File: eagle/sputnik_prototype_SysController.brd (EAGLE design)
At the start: 99 x 100 mm, 73 parts, among them IC1 74HC4067, Q1 IRLML6344TRPBF, SW1 TPS25944LRVCRWQFN-20-3X4, U1 MEGA128-A, X1 CRYSTAL-ABRACON-ABM3-SMD

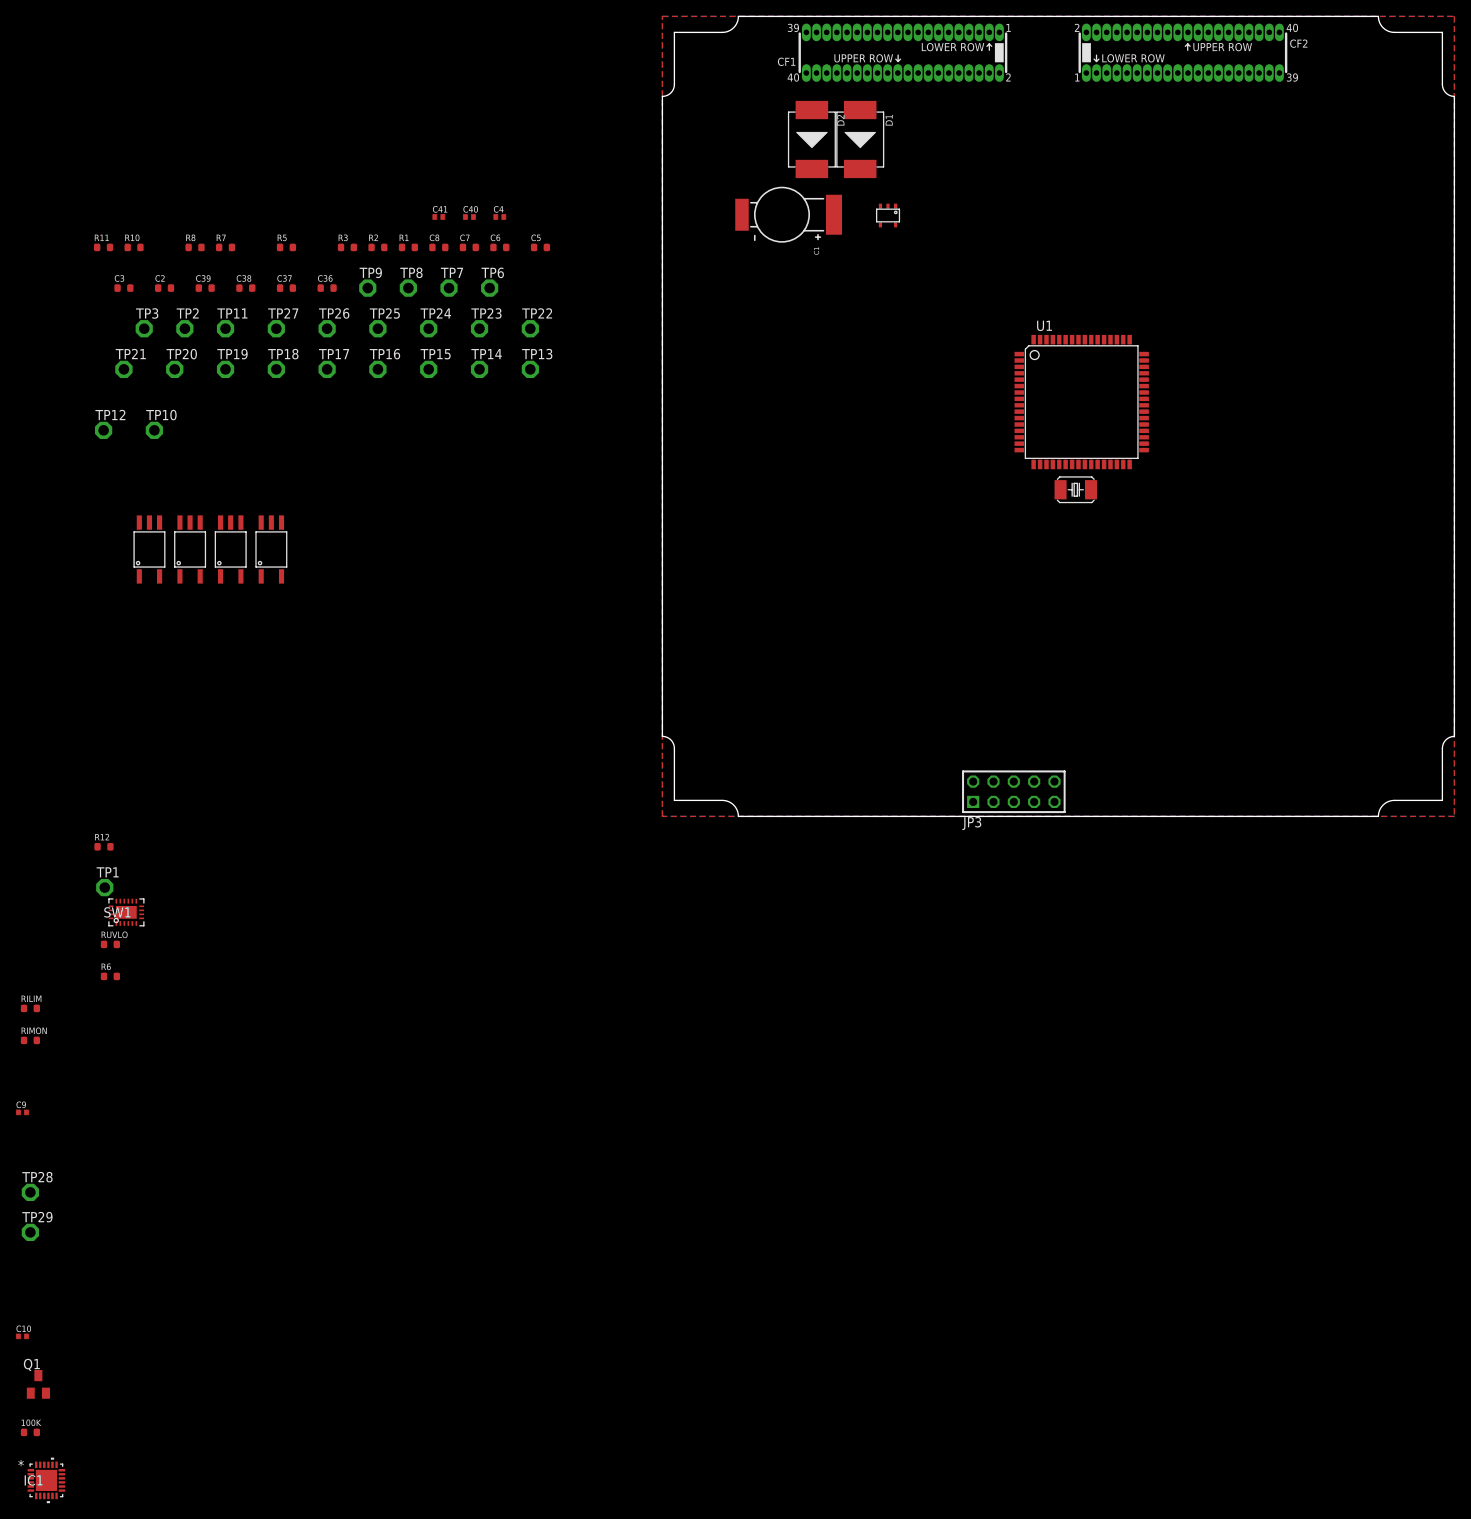
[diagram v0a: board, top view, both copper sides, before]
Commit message: Added DNP LEDs and MOSFET drives to UARTs. Fixed TPS circuits with SOT-32-6 N/P MOSFET pair, which worked out nicely. Added another TPS to flesh it out, make sure it wasn't totally stupid. Added more DN LEDs to the outputs.
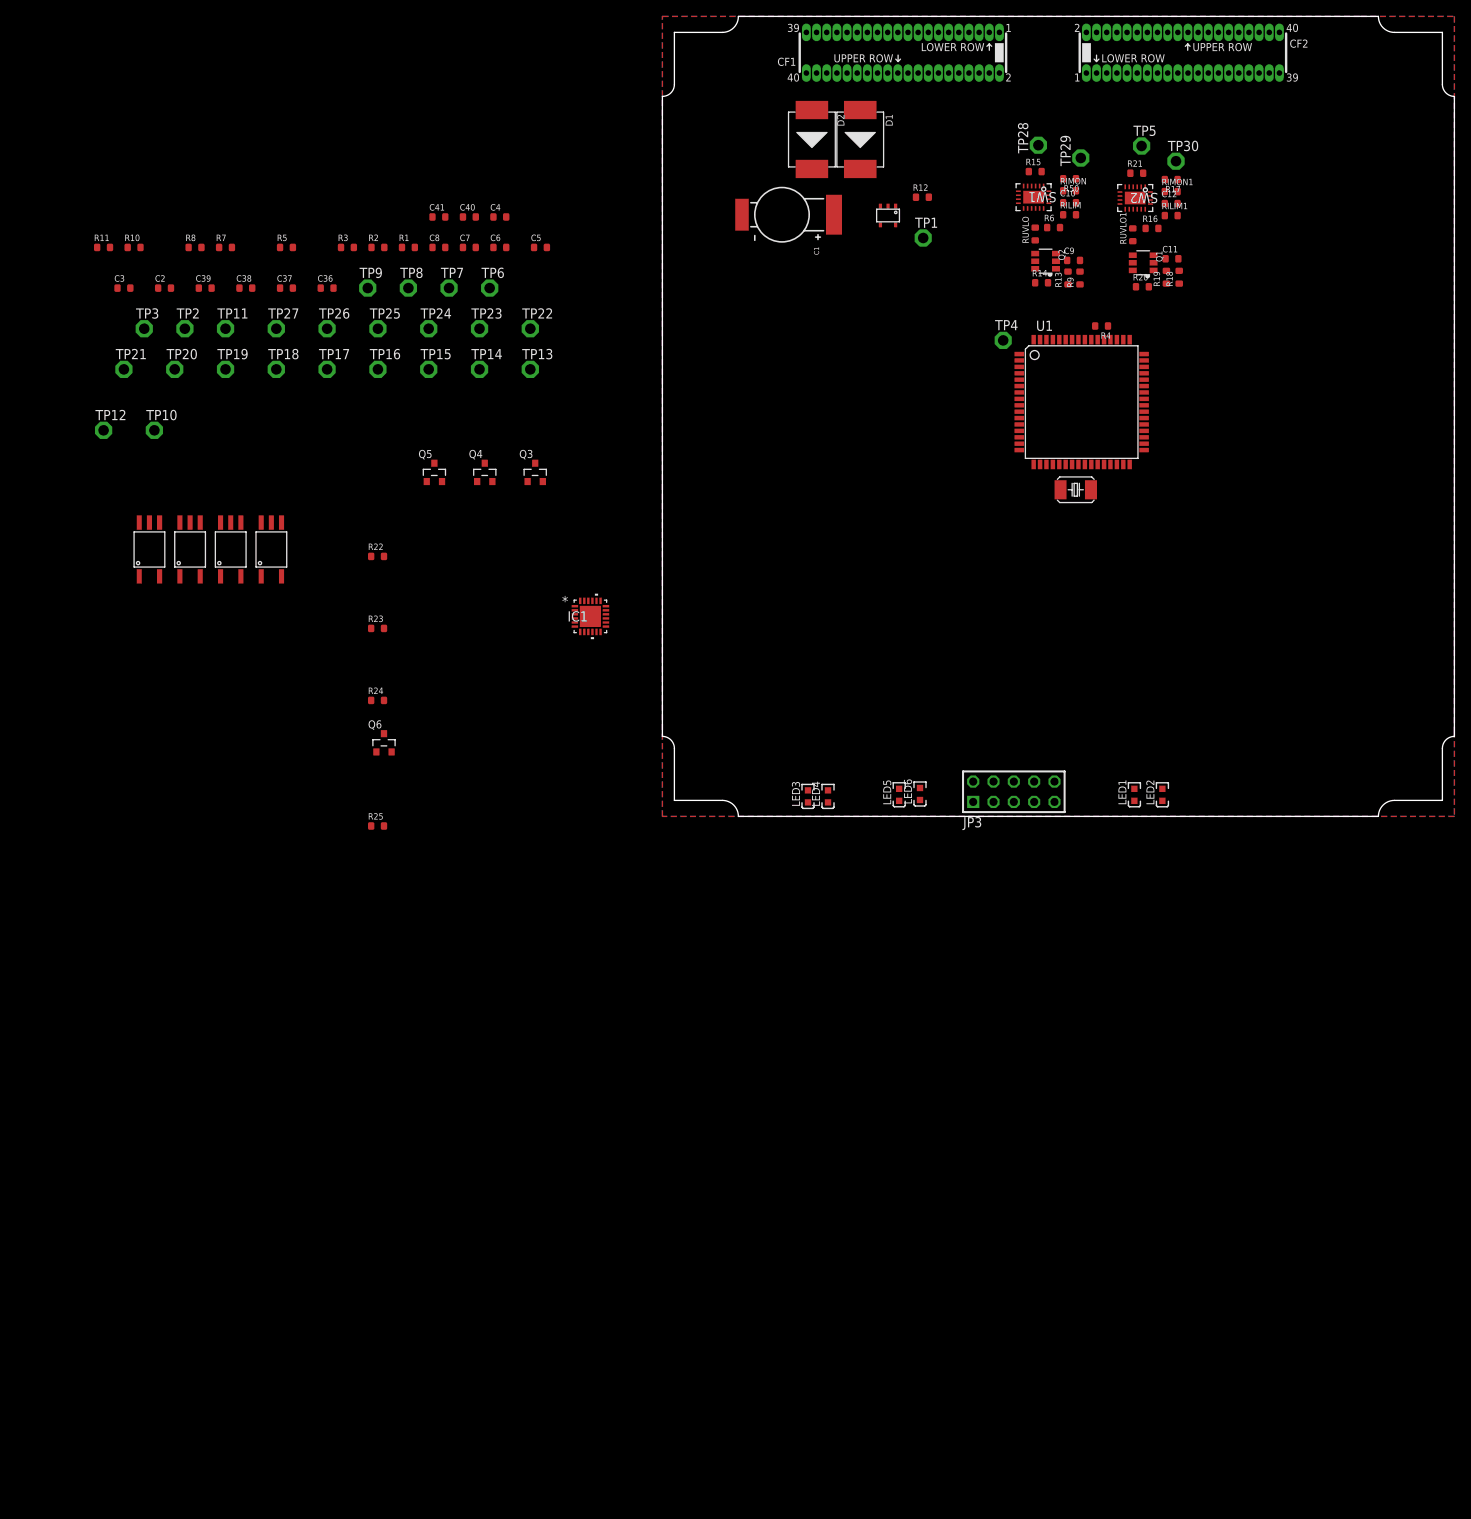
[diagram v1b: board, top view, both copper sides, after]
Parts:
- removed 100K: Value, rcl_custom:.0603-B-NOSILK
- added C11: 1uF, rcl_custom:.0603-B-NOSILK
- added C12, RILIM1, RIMON1: TBD, rcl_custom:.0603-B-NOSILK
- added LED1, LED2: GRN, psas_c3_team05:LED-0603
- added LED3, LED4, LED5, LED6: DNP/AMB, psas_c3_team05:LED-0603
- added Q2: MOSFET-P-N-PAIR, ic-transistor-mosfet-n-p:SOT23-6
- added Q3, Q4, Q5, Q6: DNP/NTR4101P, Tova:SOT23
- added R13, R14, R17, R19, R20, R50: 47k, rcl_custom:.0603-B-NOSILK
- added R15, R21: 1k, rcl_custom:.0603-B-NOSILK
- added R16, RUVLO1: Value, rcl_custom:.0603-B-NOSILK
- added R18, R9: 4.7k, rcl_custom:.0603-B-NOSILK
- added R22, R23, R24, R25: DNP/1k, rcl_custom:.0603-B-NOSILK
- added R4: 390, rcl_custom:.0603-B-NOSILK
- added SW2: TPS25944LRVCRWQFN-20-3X4, WQFN-20-3x4:QFN-20-L
- added TP30, TP4, TP5: TPSPAD1-13, testpad:P1-13
- C10: value Value -> TBD; device rcl_custom:.0402-B-NOSILK -> rcl_custom:.0603-B-NOSILK
- C4, C40, C41, C9: device rcl_custom:.0402-B-NOSILK -> rcl_custom:.0603-B-NOSILK
- Q1: value IRLML6344TRPBF -> MOSFET-P-N-PAIR; device adafruit:SOT23 -> ic-transistor-mosfet-n-p:SOT23-6
- RILIM, RIMON: value Value -> TBD
- moved Q1 196.8 mm to (60.1, 69.2), turned to 270 degrees
- moved C10 192.9 mm to (50.9, 76.7)
- moved TP29 187.8 mm to (52.3, 82.3), turned to 90 degrees
- moved TP28 181.7 mm to (47.0, 83.9), turned to 90 degrees
- moved C9 169.1 mm to (51.4, 69.5)
- moved RIMON 167.8 mm to (50.9, 78.2)
- moved RILIM 163.4 mm to (50.9, 75.2)
- moved R6 150.5 mm to (48.9, 73.6)
- moved RUVLO 145.8 mm to (46.6, 72.8), turned to 90 degrees
- moved SW1 144.4 mm to (46.4, 77.4), turned to 180 degrees
- moved R12 130.6 mm to (32.5, 77.4)
- moved TP1 130.6 mm to (32.6, 72.3)
- moved IC1 127.6 mm to (-9.00, 25.0)
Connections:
- net N$19 renamed RXD1
- net SDL renamed SCL
- removed net +3V3: C2.2, C3.2, C36.2, C37.2, C38.2, C39.2, C4.1, JP3.4, JP3.7, U$2.5, U$4.5, U$8.5, U1.21, U1.52, U1.62, U1.64
- removed net N$10: R3.2, U1.28
- removed net PA0: TP6.TP, U1.51
- removed net PA1: TP3.TP, U1.50
- removed net PC0: TP27.TP, U1.35
- removed net PC1: TP26.TP, U1.36
- removed net PTA1: R7.2, U1.3
- removed net PTA2: R8.2, U1.2
- new net 3V: C2.2, C3.2, C36.2, C37.2, C38.2, C39.2, C4.1, JP3.4, JP3.7, Q3.2, Q4.2, Q5.2, Q6.2, R17.1, R4.1, R50.1, U$2.5, U$4.5, U$8.5, U1.21, U1.52, U1.62, U1.64
- new net ILIM_ANALOG_IN: U1.61
- new net N$30: RILIM1.1, SW2.17
- new net N$32: SW2.2, TP30.TP
- new net N$33: TP4.TP, U1.1
- new net N$34: U1.58
- new net N$35: U1.59
- new net N$37: U1.60
- new net N$38: C12.1, SW2.18
- new net N$39: U1.4
- new net N$40: U1.5
- new net N$41: U1.6
- new net N$42: U1.7
- new net N$43: U1.8
- new net N$44: U1.9
- new net N$45: U1.29
- new net N$46: U1.30
- new net N$47: U1.31
- new net N$48: U1.32
- new net N$49: Q1.1, R18.2, R19.2
- new net N$50: Q1.4, RUVLO1.1
- new net N$51: Q1.3, Q1.6, R20.1
- new net N$52: LED2.A, R21.2
- new net N$53: LED3.A, R22.2
- new net N$54: Q3.3, R22.1
- new net N$55: LED4.A, R23.2
- new net N$56: Q4.3, R23.1
- new net N$57: LED5.A, R24.2
- new net N$58: Q5.3, R24.1
- new net N$60: LED6.A, R25.2
- new net N$61: Q6.3, R25.1
- new net N$7: Q2.3, Q2.6, R14.1
- new net NUCLEAROPTION0: U1.33
- new net NUCLEAROPTION1: U1.34
- new net NUCLEAROPTION2: U1.43
- new net RXD0: Q3.1, R8.2, U1.2
- new net TXD0: Q4.1, R7.2, U1.3
- new net TXD1: Q6.1, R3.2, U1.28
- new net VCB0: CF2.P$1, CF2.P$2, CF2.P$3, CF2.P$4, R15.1, SW1.4, SW1.5, SW1.6, SW1.7, SW1.8
- new net VCB0_!FLT: R50.2, SW1.20, TP27.TP, U1.35
- new net VCB0_EN: R9.1, TP6.TP, U1.51
- new net VCB0_IMON: IC1.9, RIMON.1, SW1.19
- new net VCB1: CF2.P$6, CF2.P$7, CF2.P$8, CF2.P$9, R21.1, SW2.4, SW2.5, SW2.6, SW2.7, SW2.8
- new net VCB1_!FLT: R17.2, SW2.20, TP26.TP, U1.36
- new net VCB1_EN: R18.1, TP3.TP, U1.50
- new net VCB1_IMON: RIMON1.1, SW2.19
- new net VCB2: CF2.P$11, CF2.P$12, CF2.P$13, CF2.P$14
- new net VCB3: CF2.P$16, CF2.P$17, CF2.P$18, CF2.P$19
- net GND: now also C11.2, C12.2, CF2.P$10, CF2.P$15, CF2.P$5, LED1.K, LED2.K, LED3.K, LED4.K, LED5.K, LED6.K, Q1.5, Q2.5, R13.1, R16.2, R19.1, RILIM1.2, RIMON1.2, SW1.3, SW2.1, SW2.15, SW2.16, SW2.21, SW2.3, TP28.TP, TP5.TP, U$2.2; no longer Q1.2
- net N$15: now also R4.2
- net N$2: now also Q2.1, R13.2, R9.2; no longer 100K.1, C9.1, RUVLO.1, SW1.10, SW1.11, SW1.12, SW1.13, SW1.9
- net N$26: now also LED1.A, R15.2; no longer Q1.1
- net N$27: now also U1.18; no longer RIMON.1, SW1.19
- net N$28: now also U1.19; no longer SW1.3, TP28.TP
- net N$29: now also R16.1, RUVLO1.2, SW2.14; no longer 100K.2, SW1.20
- net N$3: now also Q2.4, RUVLO.1; no longer SW1.4, SW1.5, SW1.6, SW1.7, SW1.8
- net N$9: no longer Q1.3
- net VBUS: now also C11.1, C9.1, Q1.2, Q2.2, R14.2, R20.2, SW1.10, SW1.11, SW1.12, SW1.13, SW1.9, SW2.10, SW2.11, SW2.12, SW2.13, SW2.9
